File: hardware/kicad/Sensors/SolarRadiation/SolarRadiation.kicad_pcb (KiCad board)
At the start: 2 copper layers, 43 x 27 mm, 16 parts, among them U1 ADS1115IDGS, U2 TMP100

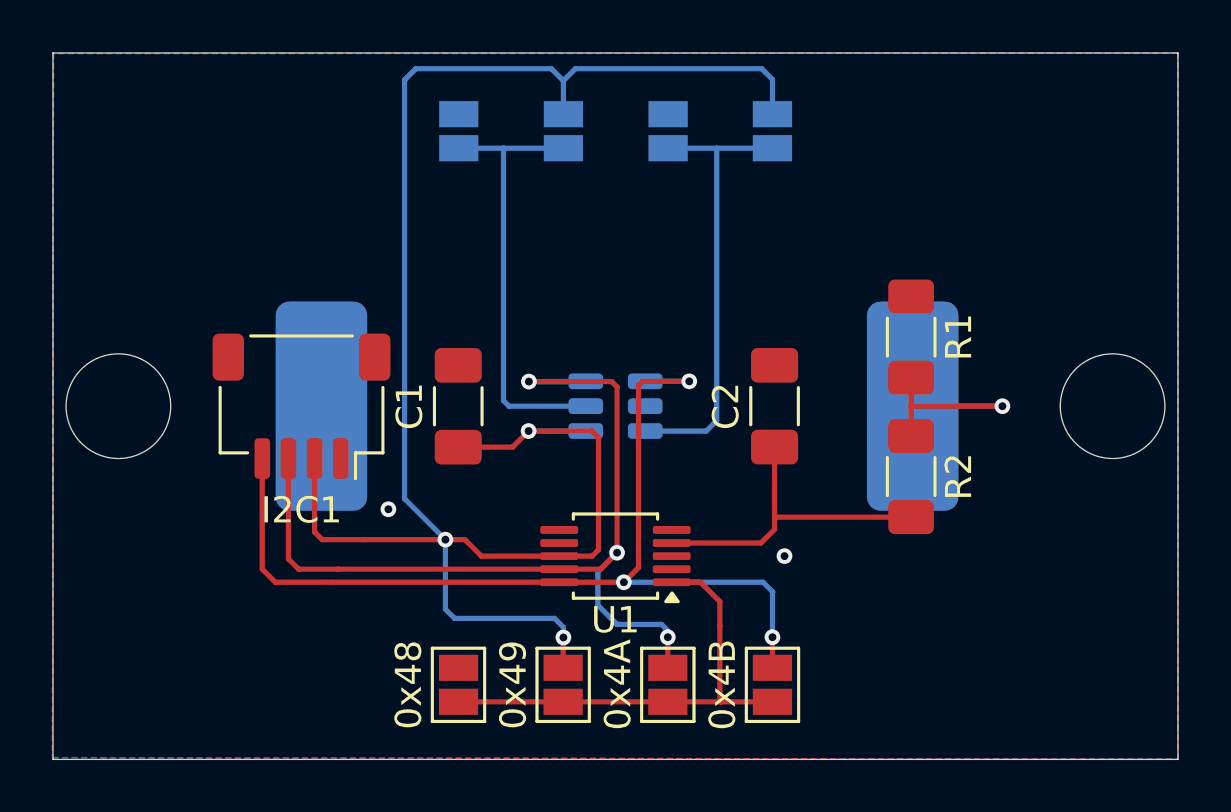
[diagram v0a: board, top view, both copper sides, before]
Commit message: Changed Footprint for R1 to THT 0207
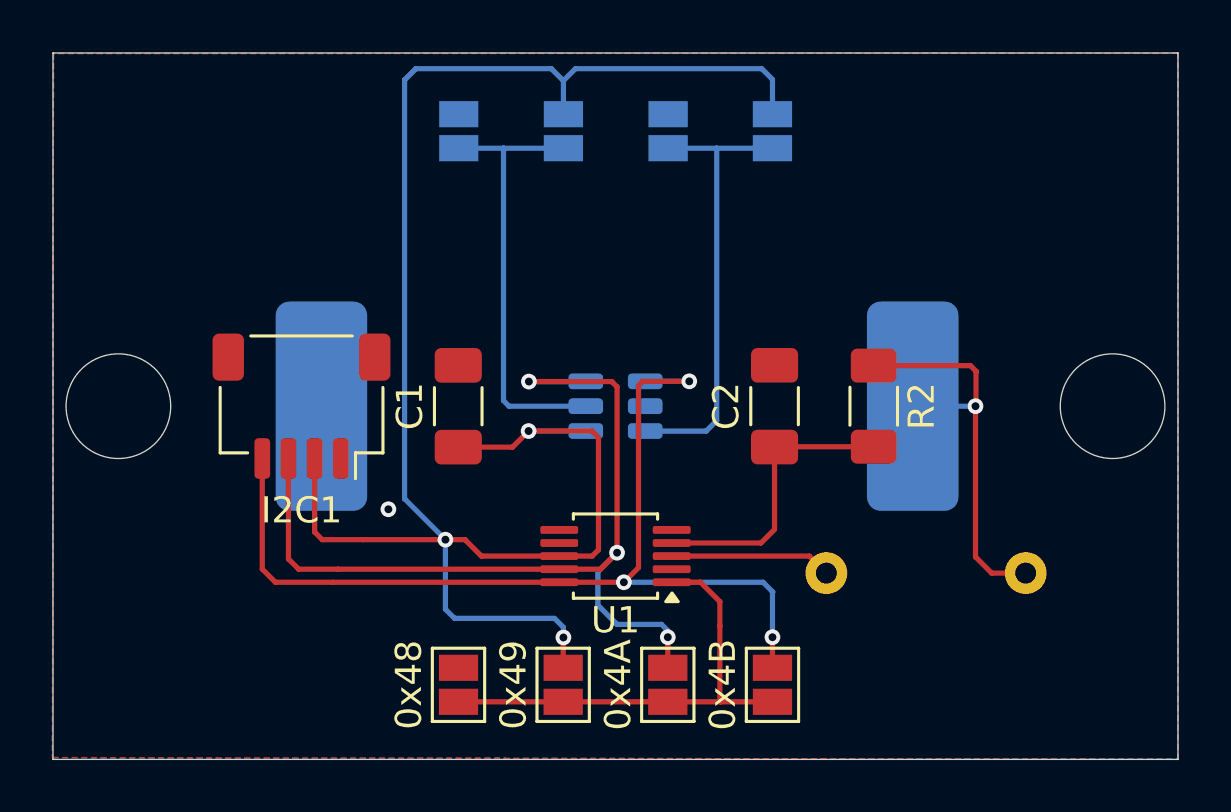
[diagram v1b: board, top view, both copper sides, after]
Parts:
- R1: footprint Resistor_SMD:R_1206_3216Metric_Pad1.30x1.75mm_HandSolder -> Resistor_THT:R_Axial_DIN0207_L6.3mm_D2.5mm_P7.62mm_Horizontal; moved to B.Cu
- SC1: footprint EnvNode:KXOB25-14X1F -> EnvNode-Footprints:KXOB25-14X1F
- moved R1 9.58 mm to (128.2, 92.4), turned to 0 degrees
- moved R2 3.05 mm to (130.1, 86.0)
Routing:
- net Net-(SC1-+): track 9.15 -> 15.7 mm
- net GND: track 0.00 -> 6.18 mm, vias 2 -> 1
- net Net-(U1-AIN0): track 12.6 -> 11.1 mm

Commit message: fix(hardware): move SolarRadiation shunt to front and update jumpers
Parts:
- removed JP7: A1-V, Jumper:SolderJumper-2_P1.3mm_Open_Pad1.0x1.5mm
- removed JP8: A1-G, Jumper:SolderJumper-2_P1.3mm_Open_Pad1.0x1.5mm
- JP5: value A0-V -> SolderJumper_3_Open; footprint Jumper:SolderJumper-2_P1.3mm_Open_Pad1.0x1.5mm -> Jumper:SolderJumper-3_P1.3mm_Open_RoundedPad1.0x1.5mm_NumberLabels
- JP6: value A0-G -> SolderJumper_3_Open; footprint Jumper:SolderJumper-2_P1.3mm_Open_Pad1.0x1.5mm -> Jumper:SolderJumper-3_P1.3mm_Open_RoundedPad1.0x1.5mm_NumberLabels
- R1: moved to F.Cu
- moved JP6 7.91 mm to (121.9, 77.2), turned to 90 degrees
- moved JP5 1.74 mm to (118.4, 77.2), turned to 90 degrees
- renumbered C2 to C1, C1 to C2
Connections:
- JP6 pad 1: GND -> +3V3
- JP6 pad 2: ADD0 -> ADD1
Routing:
- net +3V3: track 71.1 -> 48.2 mm
- net ADD1: track 17.3 -> 14.2 mm
- net ADD0: track 16.9 -> 14.1 mm
- net GND: vias 1 -> 3
